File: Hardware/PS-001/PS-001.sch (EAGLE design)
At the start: 109 parts, among them J1 10144517-042802LF, J2 10144518-041802LF, J3 10144517-042802LF, J4 10144518-041802LF, J6 2X5_0.05_SWD, Q1 STD15P6F6AG, Q2 DMP3018SFVQ-13, Q3 DMP3018SFVQ-13, U1 ATSAMC21E15A-AUT, U2 MAX16935CAUES/V+, U3 MAX16935CAUES/V+, U4 INA186A2IDCKT, U5 INA2180A4IDGKR, U6 NCV8170AXV330T2G, U7 ATA6561-GAQW-N, U8 LM2902DT, U9 LM2902DT

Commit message: updated sch with atsamC21G - brd needs work
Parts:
- removed C33, C34, C35: 100nF, rcl:C-EUC0402
- removed D3: (no value), adafruit:DIODESOD-123
- removed R29: 10k, rcl:R-US_R0402
- removed U1: ATSAMC21E15A-AUT, SamacSys_Parts:ATSAMC21E15A-AUT
- added C46: 1uF, rcl:C-EUC0805
- added C47, C48, C49: 100nF, rcl:C-EUC0805
- added C50, C51, C52: 100nF, rcl:C-EUC0402
- added D4: (no value), adafruit:DIODESOD-123
- added R32: 10k, rcl:R-US_R0402
- added U$60: ATSAMC21G17A-AUT, ATSAM:ATSAMC21G17A-AUT
- C32: value 1uF -> 100nF
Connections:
- removed net N$20: D3.A, U1A.PA28
- new net N$29: C46.1, C47.1, U$60G$1.VDDCORE
- new net N$30: D4.A, U$60G$2.PA12
- net +3.3V_INT_VMON: now also U$60G$2.PA09; no longer U1A.PA11/SERCOM0/PAD3/SCK/AIN11
- net +3.5V_IMON: now also C52.1, U$60G$2.PA06; no longer C33.1, U1A.PA08/SERCOM0/PAD0/MISO/SDA/AIN8
- net +3.5V_INT_VMON: now also U$60G$2.PA03; no longer U1A.PA03/AIN1
- net +3.5V_VMON: now also U$60G$2.PB09; no longer U1A.PA05/AIN5
- net +3V3: now also C48.1, C49.1, U$60G$1.VDDANA, U$60G$1.VDDIN, U$60G$1.VDDIO_1, U$60G$1.VDDIO_2; no longer U1B.VDDANA, U1B.VDDCORE, U1B.VDDIN
- net +5V_IMON: now also C51.1, U$60G$2.PA07; no longer C34.1, U1A.PA09/SERCOM0/PAD1/SS/SCL/AIN9
- net +5V_INT_VMON: now also U$60G$2.PA04; no longer U1A.PA06/AIN6
- net +5V_VMON: now also U$60G$2.PA05; no longer U1A.PA07/AIN7
- net +V_BAT_IMON: now also C50.1, U$60G$2.PA08; no longer C35.1, U1A.PA10/SERCOM0/PAD2/MOSI/AIN10
- net +V_BAT_INT_VMON: now also U$60G$2.PA02; no longer U1A.PA02/AIN0/DAC
- net +V_BAT_VMON: now also U$60G$2.PB08; no longer U1A.PA04/AIN4
- net CANRX: now also U$60G$2.PA25; no longer U1A.PA25/SERCOM3/PAD3/CAN0RX
- net CANTX: now also U$60G$2.PA24; no longer U1A.PA24/SERCOM3/PAD2/CAN0TX
- net CAN_STBY: now also U$60G$2.PA27; no longer U1A.PA27
- net DETECT_A: now also U$60G$2.PA13; no longer U1A.PA00
- net DETECT_B: now also U$60G$2.PA14; no longer U1A.PA01
- net DGND: now also C46.2, C47.2, C48.2, C49.2, C50.2, C51.2, C52.2, U$60G$1.GNDANA, U$60G$1.GND_1, U$60G$1.GND_2, U$60G$1.GND_3; no longer C33.2, C34.2, C35.2, U1B.GND_1, U1B.GND_2
- net PGND: now also R32.1; no longer R29.1
- net PGOOD_+3.5V: now also U$60G$2.PB10; no longer U1A.PA14
- net PGOOD_+5V: now also U$60G$2.PB11; no longer U1A.PA15
- net P_GOOD: now also D4.C, R32.2; no longer D3.C, R29.2
- net RESET: now also U$60G$1.!RESET; no longer U1B.!RESET
- net SWCLK: now also U$60G$1.PA30/SWCLK; no longer U1B.PA30/SWCLK
- net SWDIO: now also U$60G$1.PA31/SWDIO; no longer U1B.PA31/SWDIO

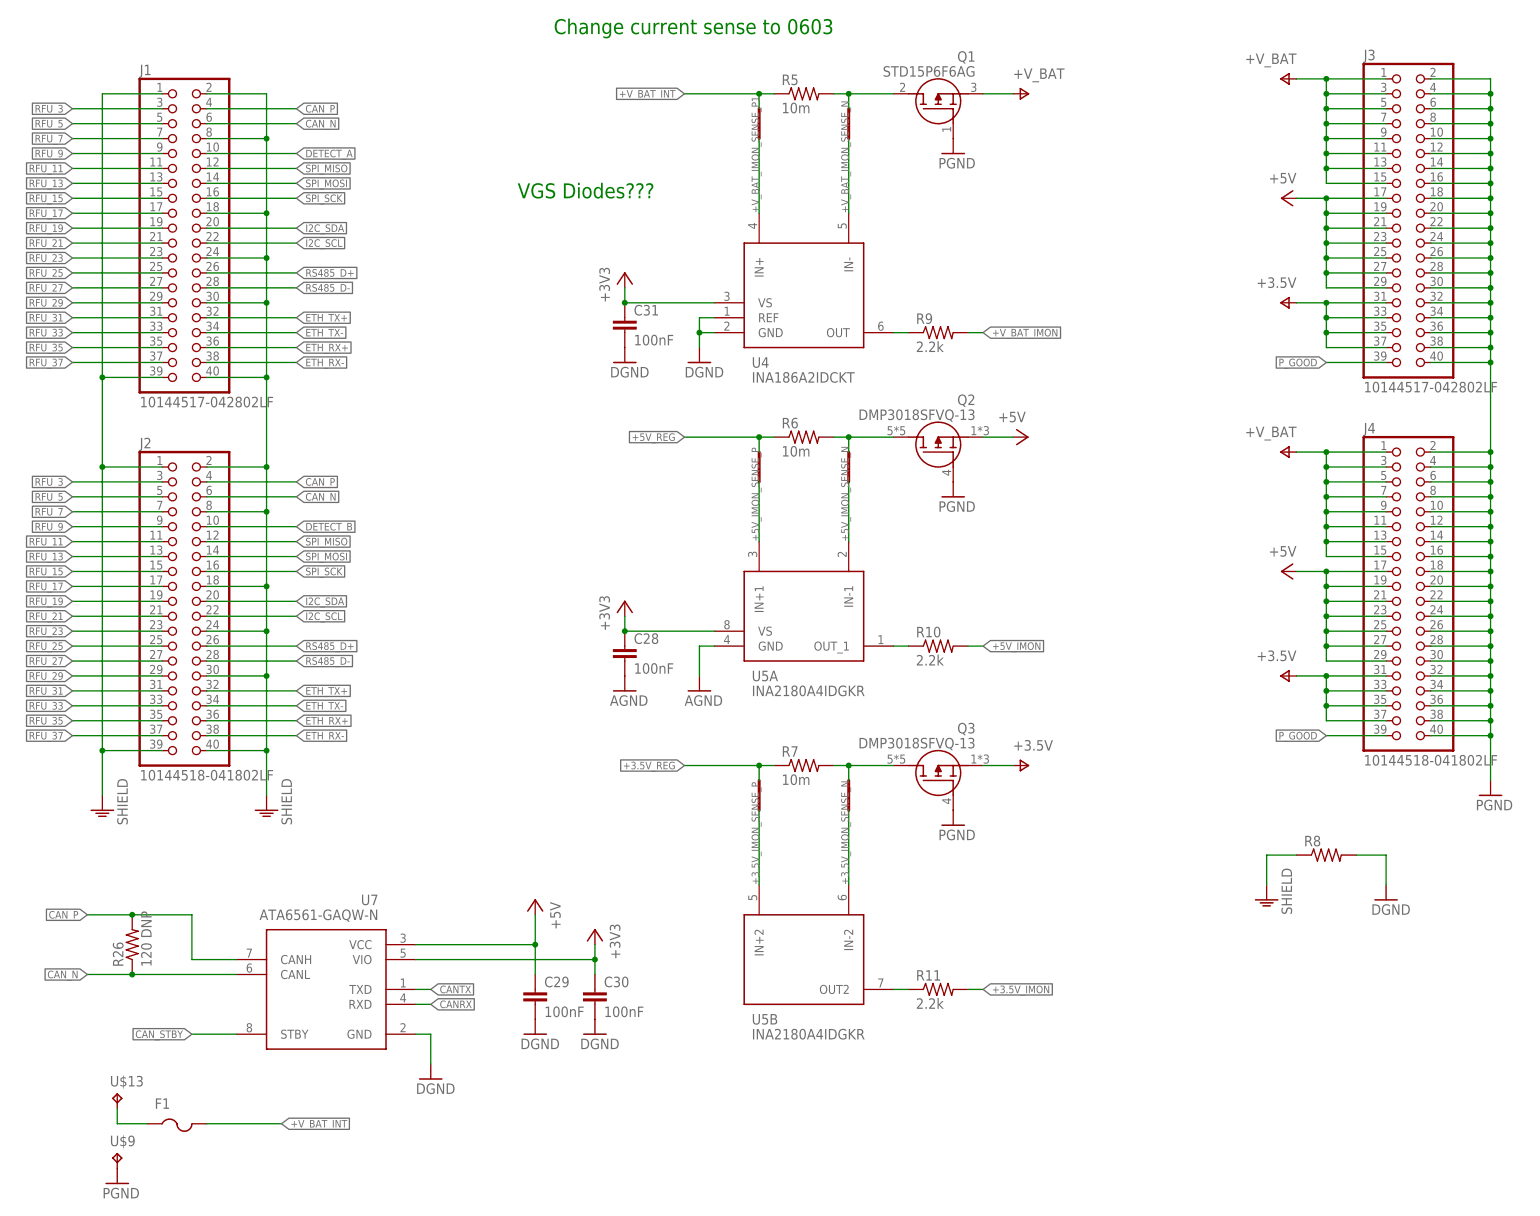
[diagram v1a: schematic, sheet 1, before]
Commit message: updating voltage rails, should we get rid of
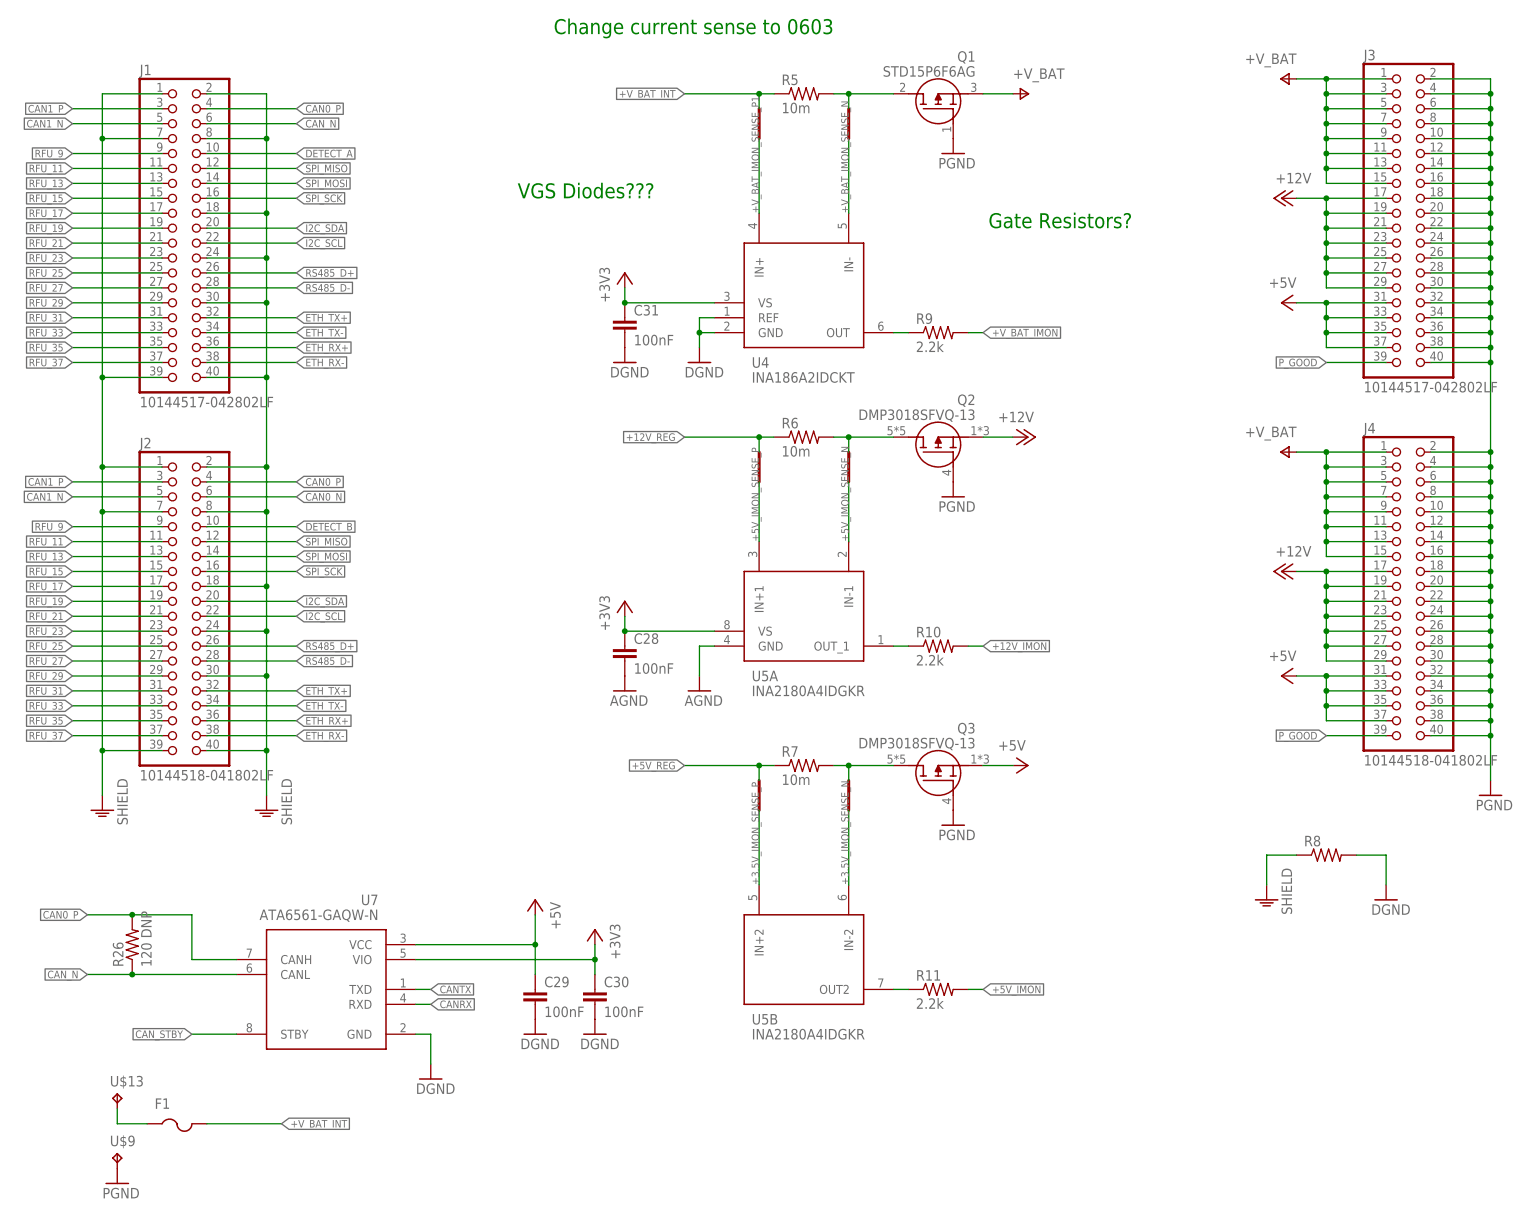
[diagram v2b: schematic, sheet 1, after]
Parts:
- added R29: 5.6k, rcl:R-US_R0402
- added R33: 2.2k, rcl:R-US_R0402
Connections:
- net +3.5V_FB renamed +5V_FB
- net CAN_P renamed CAN0_P
- net N$22 renamed VBIAS_U3
- net RFU_3 renamed CAN1_P
- net RFU_5 renamed CAN1_N
- removed net +3.5V_IMON: C52.1, R11.2, U$60G$2.PA06
- removed net +3.5V_REG: C16.1, C17.1, C18.1, L2.2, R12.2, R27.2, R7.1, SH1.P$2, U3.OUT
- removed net RFU_7: J1.7, J2.7
- new net +12V: J3.17, J3.19, J3.21, J3.23, J3.25, J3.27, J3.29, J4.17, J4.19, J4.21, J4.23, J4.25, J4.27, J4.29, Q2.S
- new net +12V_FB: R29.1, R33.2
- new net +12V_IMON: C51.1, R10.2, U$60G$2.PA07
- new net +12V_REG: C4.1, C5.1, C6.1, L1.2, R16.2, R29.2, R6.1, SH3.P$2, U2.OUT
- new net CAN0_N: J2.6
- net +3.5V: no longer C1.1, J3.31, J3.33, J3.35, J3.37, J4.31, J4.33, J4.35, J4.37, Q3.S, U6.EN, U6.IN
- net +5V: now also C1.1, J3.31, J3.33, J3.35, J3.37, J4.31, J4.33, J4.35, J4.37, Q3.S, U6.EN, U6.IN; no longer J3.17, J3.19, J3.21, J3.23, J3.25, J3.27, J3.29, J4.17, J4.19, J4.21, J4.23, J4.25, J4.27, J4.29, Q2.S
- net +5V_IMON: now also C52.1, R11.2, U$60G$2.PA06; no longer C51.1, R10.2, U$60G$2.PA07
- net +5V_REG: now also C16.1, C17.1, C18.1, L2.2, R12.2, R27.2, R7.1, SH1.P$2, U3.OUT; no longer C4.1, C5.1, C6.1, L1.2, R16.2, R6.1, SH3.P$2, U2.OUT
- net CAN_N: no longer J2.6
- net GND1: now also R33.1
- net SHIELD: now also J1.7, J2.7
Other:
- note added: "Gate Resistors?"
- note added: "Recalculate voltage dividers for new rail voltages"
- note added: "recalculate voltage divider for FB"
- note added: "replace FB voltage drivider with fixed output for 5V?"
- note added: "should we just get rid of the voltage following opamps? they aren't adding much value, but taking up lots of board space"

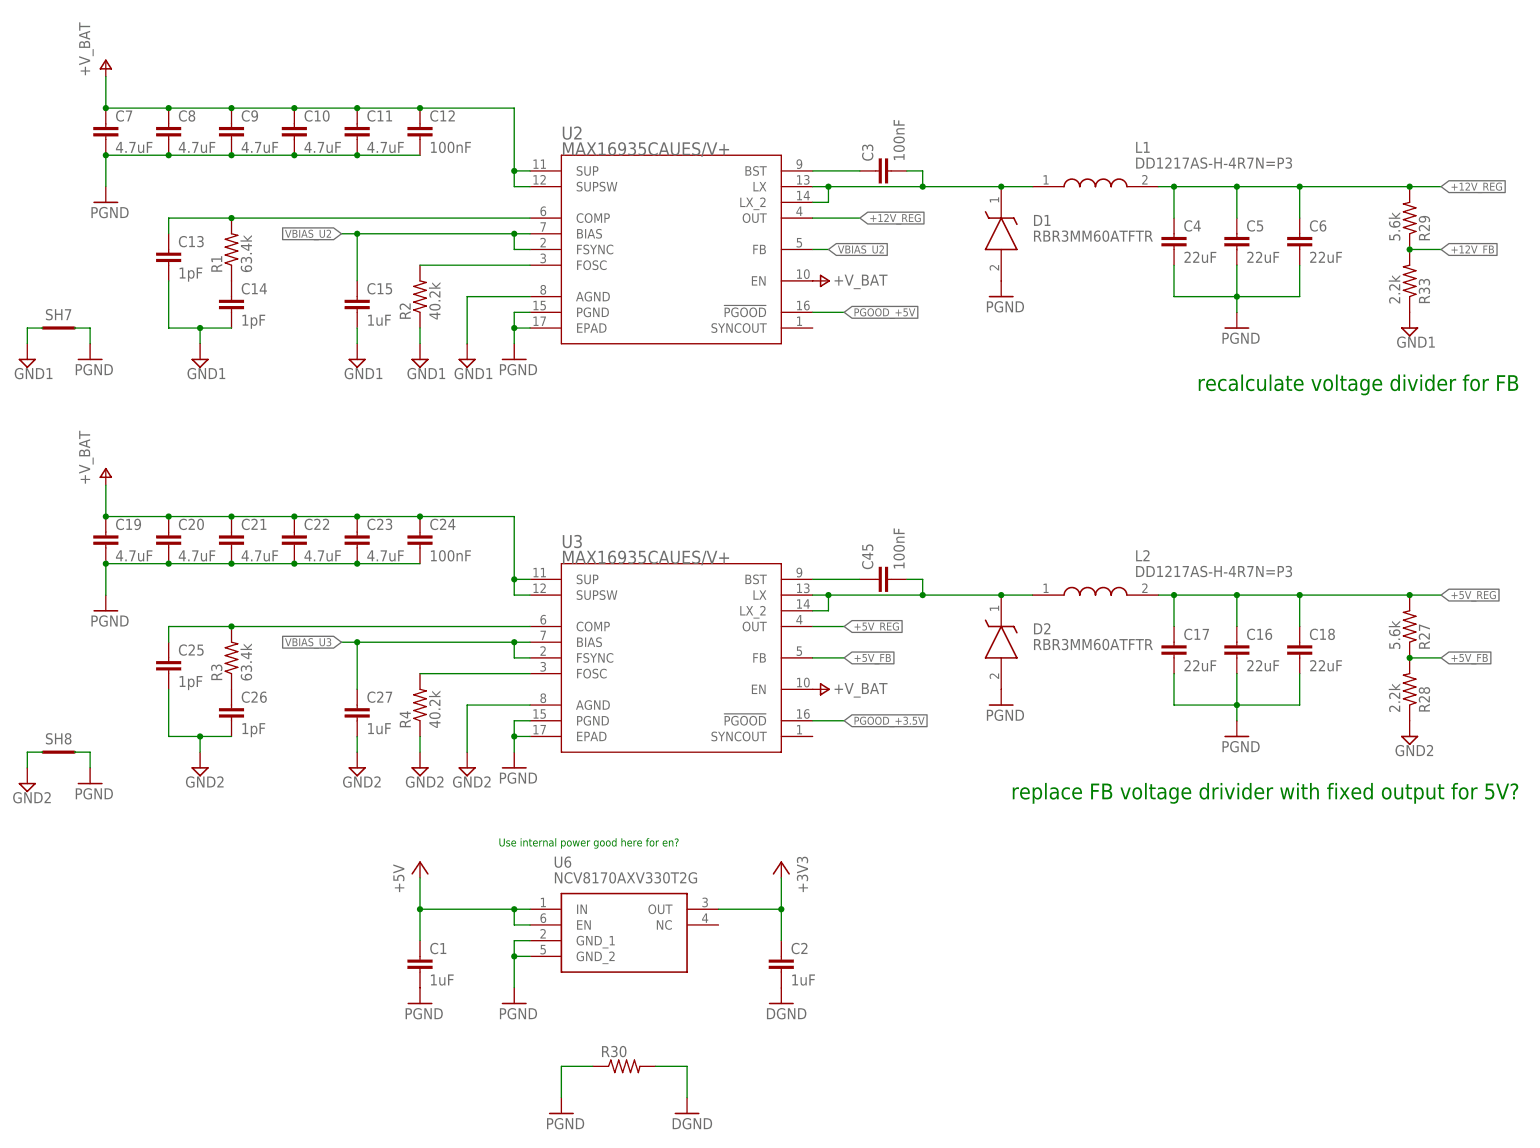
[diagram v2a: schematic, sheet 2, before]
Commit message: added some note to ps-001 sch
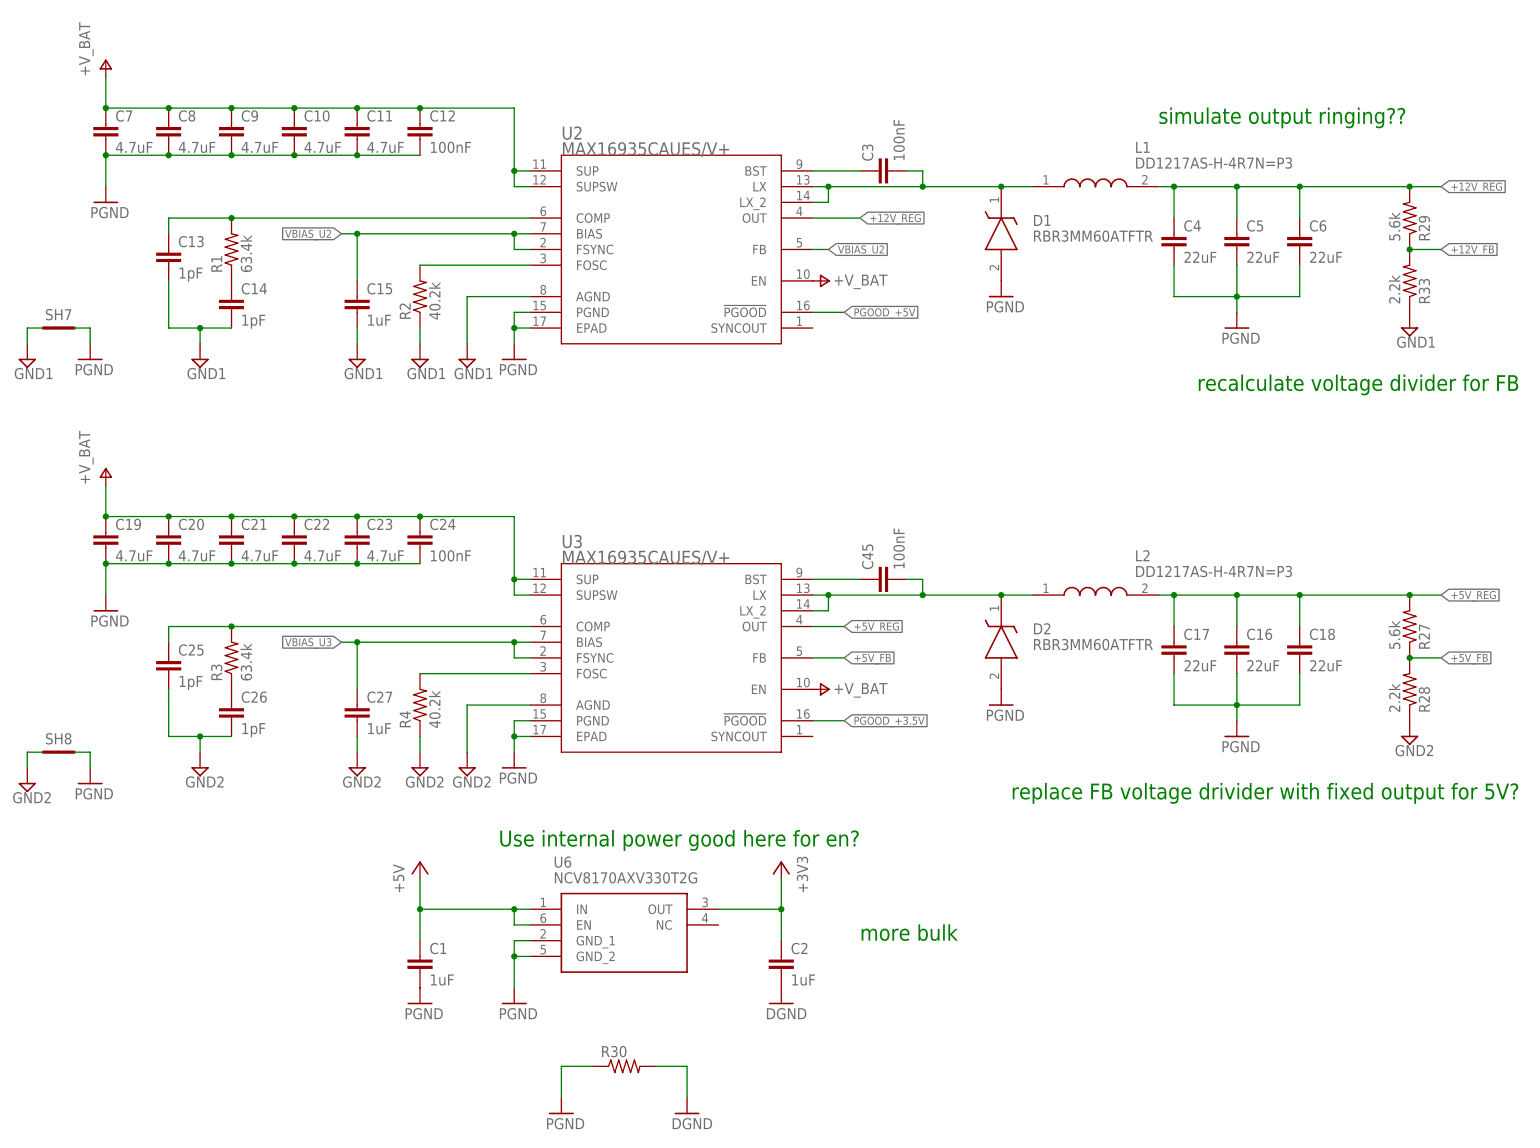
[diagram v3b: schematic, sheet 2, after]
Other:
- note added: "Fix rail names here"
- note added: "add 1k pullup on swclk"
- note added: "more bulk"
- note added: "simulate output ringing??"
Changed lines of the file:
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@@
 <sheet>
 <plain>
-<text x="99.06" y="66.04" size="1.27" layer="91">Use internal power good here for en?</text>
+<text x="99.06" y="66.04" size="2.54" layer="91">Use internal power good here for en?</text>
 <text x="264.16" y="139.7" size="2.54" layer="91" rot="MR0">recalculate voltage divider for FB</text>
 <text x="264.16" y="73.66" size="2.54" layer="91" rot="MR0">replace FB voltage drivider with fixed output for 5V?</text>
+<text x="157.48" y="50.8" size="2.54" layer="91">more bulk</text>
+<text x="205.74" y="182.88" size="2.54" layer="91">simulate output ringing??</text>
 </plain>
 <instances>
@@
 <sheet>
 <plain>
+<text x="106.68" y="116.84" size="2.54" layer="91" ratio="10">Fix rail names here</text>
+<text x="149.86" y="193.04" size="2.54" layer="91" ratio="10">add 1k pullup on swclk</text>
 </plain>
 <instances>
